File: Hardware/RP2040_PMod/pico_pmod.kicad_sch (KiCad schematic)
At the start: 39 parts, among them J1 Conn_02x06_Odd_Even, J2 Conn_02x06_Odd_Even, J3 Conn_02x06_Odd_Even, J4 USB_C_Receptacle_USB2.0, J5 Conn_01x04, SW1 SW_Push, SW2 SW_Push, U1 RP2040, U2 W25Q128JVS, U3 NCP1117-3.3_SOT223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

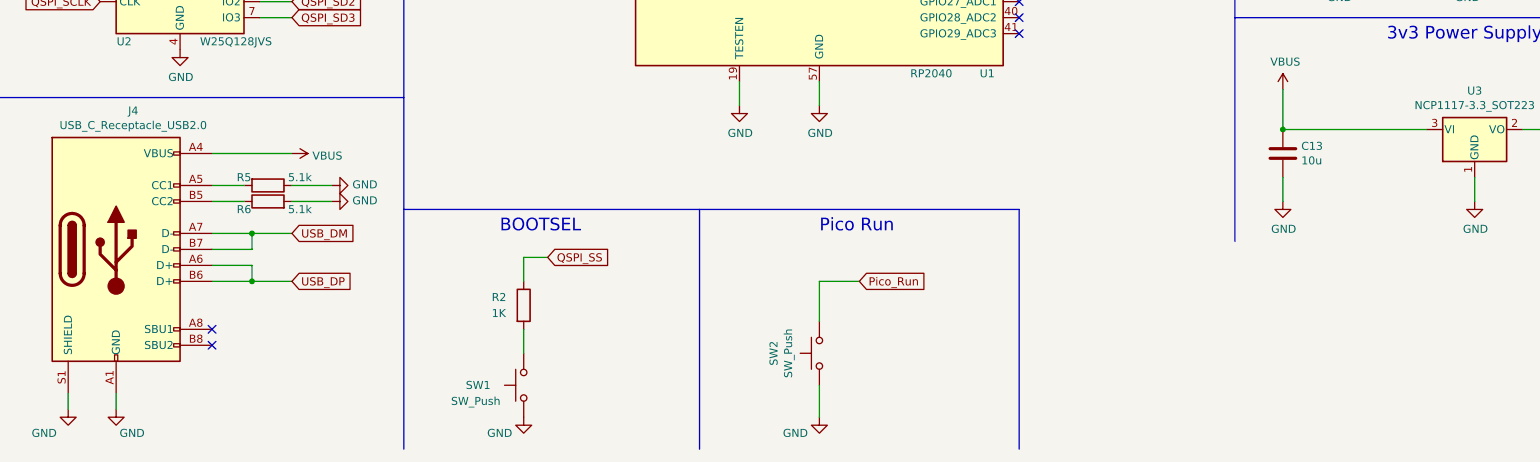
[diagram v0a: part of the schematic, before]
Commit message: add power flags to schematic for ERC
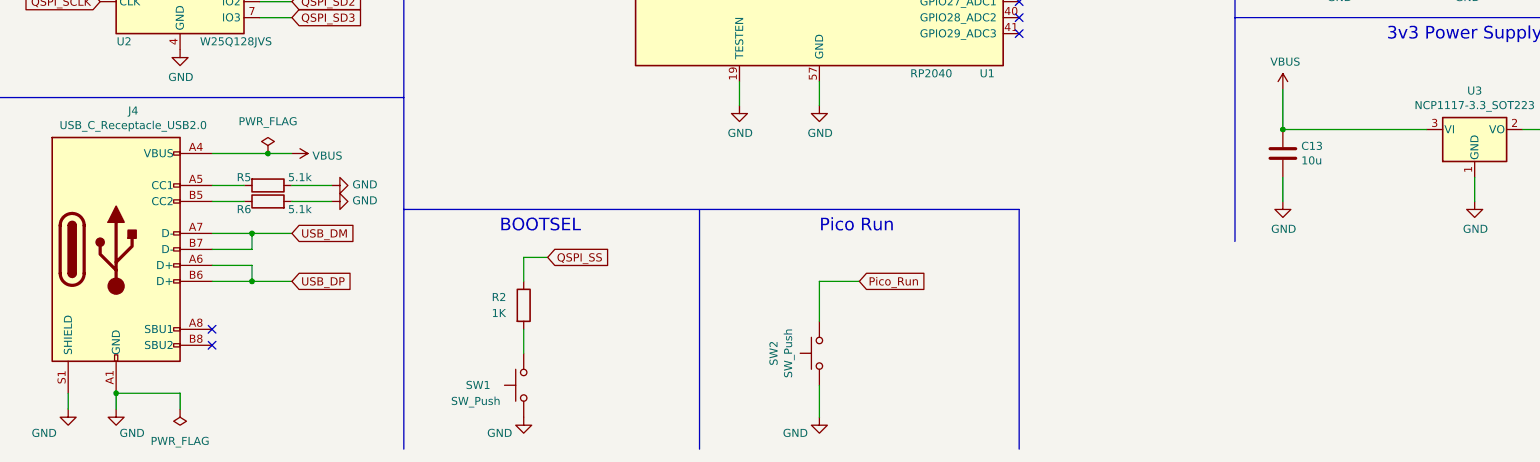
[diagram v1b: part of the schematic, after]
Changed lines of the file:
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@@
   (junction (at 33.02 78.74) (diameter 0) (color 0 0 0 0)
   )
+  (junction (at 57.15 151.13) (diameter 0) (color 0 0 0 0)
+  )
   (junction (at 26.67 102.87) (diameter 0) (color 0 0 0 0)
   )
@@
   )
   (junction (at 93.98 19.05) (diameter 0) (color 0 0 0 0)
+  )
+  (junction (at 33.02 189.23) (diameter 0) (color 0 0 0 0)
   )
   (no_connect (at 176.53 132.08))
@@
     (stroke (width 0) (type default) (color 0 0 0 0))
   )
-  (wire (pts (xy 60.96 151.13) (xy 48.26 151.13))
+  (wire (pts (xy 48.26 151.13) (xy 57.15 151.13))
     (stroke (width 0) (type default) (color 0 0 0 0))
   )
@@
     (stroke (width 0) (type default) (color 0 0 0 0))
   )
+  (wire (pts (xy 256.54 147.32) (xy 275.59 147.32))
+    (stroke (width 0) (type default) (color 0 0 0 0))
+  )
   (wire (pts (xy 255.27 22.86) (xy 264.16 22.86))
     (stroke (width 0) (type default) (color 0 0 0 0))
@@
     (stroke (width 0) (type default) (color 0 0 0 0))
   )
-  (wire (pts (xy 241.3 147.32) (xy 218.44 147.32))
-    (stroke (width 0) (type default) (color 0 0 0 0))
-  )
   (wire (pts (xy 60.96 171.45) (xy 54.61 171.45))
     (stroke (width 0) (type default) (color 0 0 0 0))
@@
     (stroke (width 0) (type default) (color 0 0 0 0))
   )
+  (wire (pts (xy 43.18 189.23) (xy 33.02 189.23))
+    (stroke (width 0) (type default) (color 0 0 0 0))
+  )
   (wire (pts (xy 124.46 38.1) (xy 124.46 21.59))
     (stroke (width 0) (type default) (color 0 0 0 0))
@@
     (stroke (width 0) (type default) (color 0 0 0 0))
   )
+  (wire (pts (xy 218.44 147.32) (xy 241.3 147.32))
+    (stroke (width 0) (type default) (color 0 0 0 0))
+  )
   (wire (pts (xy 242.57 80.01) (xy 232.41 80.01))
     (stroke (width 0) (type default) (color 0 0 0 0))
@@
     (stroke (width 0) (type default) (color 0 0 0 0))
   )
+  (wire (pts (xy 43.18 191.77) (xy 43.18 189.23))
+    (stroke (width 0) (type default) (color 0 0 0 0))
+  )
   (wire (pts (xy 127 38.1) (xy 127 20.32))
     (stroke (width 0) (type default) (color 0 0 0 0))
@@
     (stroke (width 0) (type default) (color 0 0 0 0))
   )
+  (wire (pts (xy 57.15 151.13) (xy 60.96 151.13))
+    (stroke (width 0) (type default) (color 0 0 0 0))
+  )
   (wire (pts (xy 101.6 167.64) (xy 97.79 167.64))
     (stroke (width 0) (type default) (color 0 0 0 0))
@@
   )
   (wire (pts (xy 40.64 27.94) (xy 35.56 27.94))
-    (stroke (width 0) (type default) (color 0 0 0 0))
-  )
-  (wire (pts (xy 256.54 147.32) (xy 275.59 147.32))
     (stroke (width 0) (type default) (color 0 0 0 0))
   )
@@
     (pin "1")
   )
+  (symbol (lib_id "power:PWR_FLAG") (at 57.15 151.13 0) (unit 1)
+    (in_bom yes) (on_board yes) (fields_autoplaced)
+    (property "Reference" "#FLG0102" (id 0) (at 57.15 149.225 0)
+      (effects (font (size 1.27 1.27)) hide)
+    )
+    (property "Value" "PWR_FLAG" (id 1) (at 57.15 146.05 0))
+    (property "Footprint" "" (id 2) (at 57.15 151.13 0)
+      (effects (font (size 1.27 1.27)) hide)
+    )
+    (property "Datasheet" "~" (id 3) (at 57.15 151.13 0)
+      (effects (font (size 1.27 1.27)) hide)
+    )
+    (pin "1")
+  )
+  (symbol (lib_id "power:PWR_FLAG") (at 43.18 191.77 180) (unit 1)
+    (in_bom yes) (on_board yes) (fields_autoplaced)
+    (property "Reference" "#FLG0101" (id 0) (at 43.18 193.675 0)
+      (effects (font (size 1.27 1.27)) hide)
+    )
+    (property "Value" "PWR_FLAG" (id 1) (at 43.18 196.85 0))
+    (property "Footprint" "" (id 2) (at 43.18 191.77 0)
+      (effects (font (size 1.27 1.27)) hide)
+    )
+    (property "Datasheet" "~" (id 3) (at 43.18 191.77 0)
+      (effects (font (size 1.27 1.27)) hide)
+    )
+    (pin "1")
+  )
   (sheet_instances
     (path "/" (page "1"))
   )
   (symbol_instances
+    (path "/ea875e74-ca6f-4a31-a519-44c018b1720e"
+      (reference "#FLG0101") (unit 1) (value "PWR_FLAG") (footprint "")
+    )
+    (path "/94680b10-1536-421d-a7e5-c7a3c30c89ed"
+      (reference "#FLG0102") (unit 1) (value "PWR_FLAG") (footprint "")
+    )
     (path "/00000000-0000-0000-0000-000060ea87f5"
       (reference "#PWR0101") (unit 1) (value "GND") (footprint "")

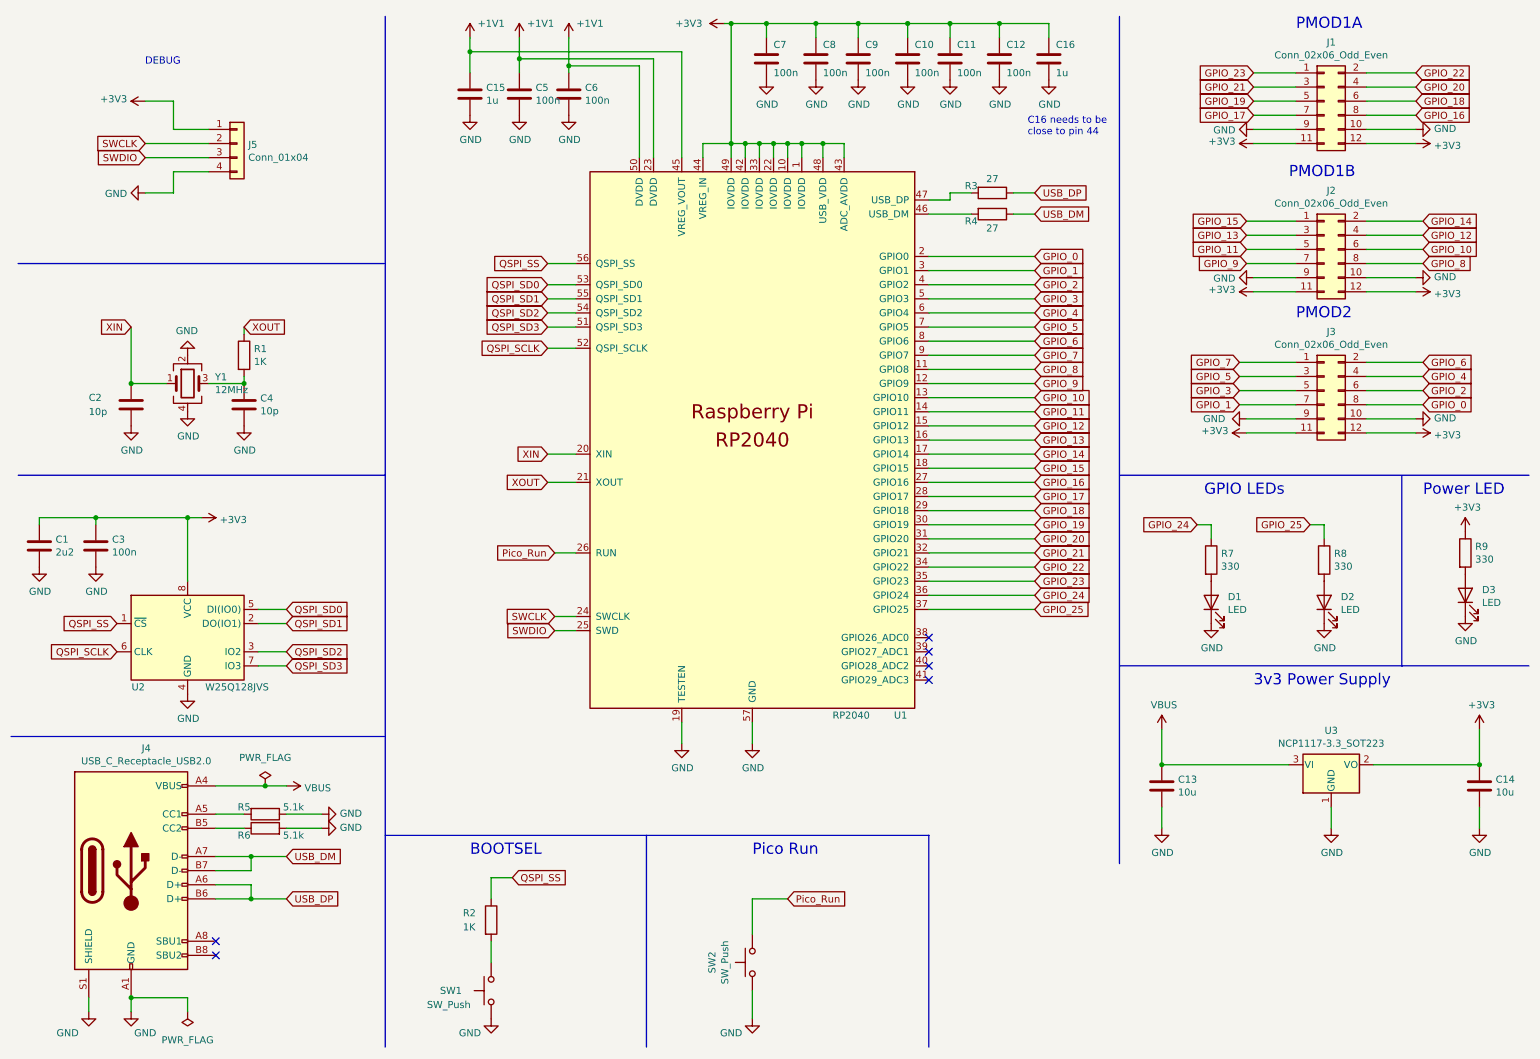
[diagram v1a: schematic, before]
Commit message: Update schematic to kicad7
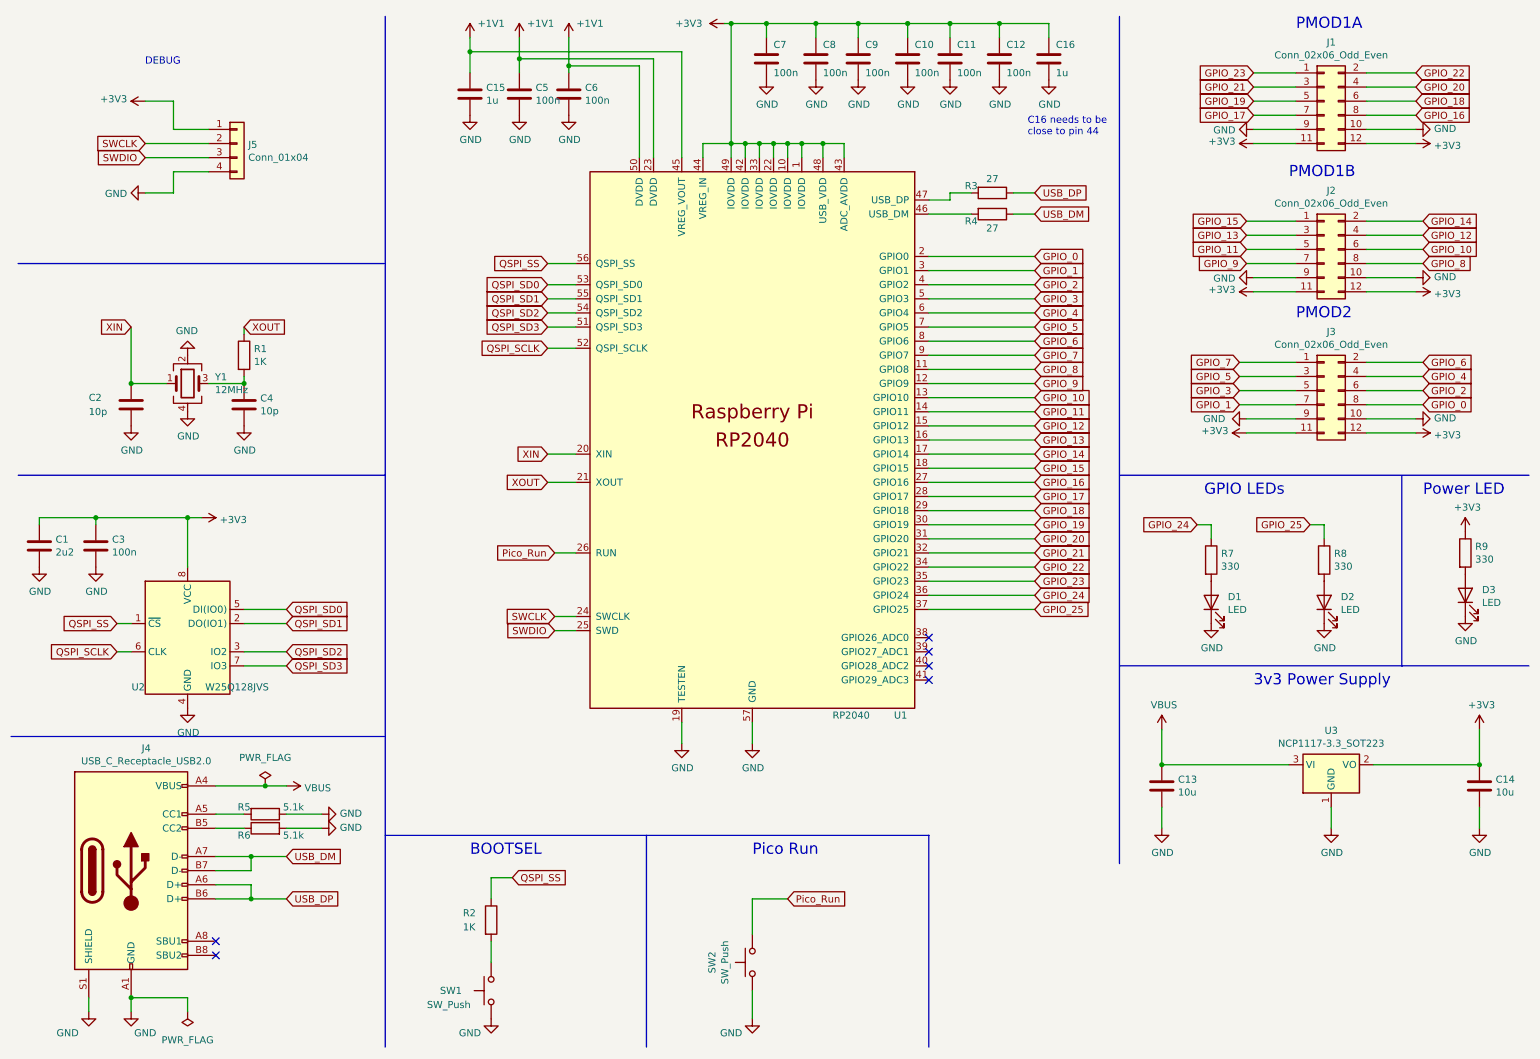
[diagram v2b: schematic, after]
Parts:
- U1: footprint RaspberryPi:RP2040-QFN-56 -> RP2040_minimal:RP2040-QFN-56

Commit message: Add JLC Part numbers
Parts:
- J1, J2, J3, J5, SW1, SW2: now left out of the parts list
- J4: JLC (none) -> C5119948
- R2: JLC (none) -> C21190
- R5, R6: JLC (none) -> C23186
- U1: JLC (none) -> C2040
- U2: JLC (none) -> C97521
- U3: JLC (none) -> C146799
- Y1: JLC (none) -> C5765982
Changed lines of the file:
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@@
+      (effects (font (size 1.27 1.27)) hide)
+    )
+    (property "JLC" "C2040" (at 144.78 88.9 0)
       (effects (font (size 1.27 1.27)) hide)
     )
@@
   )
   (symbol (lib_id "Connector_Generic:Conn_02x06_Odd_Even") (at 247.65 27.94 0) (unit 1)
-    (in_bom yes) (on_board yes) (dnp no)
+    (in_bom no) (on_board yes) (dnp no)
     (property "Reference" "J1" (at 248.92 17.3482 0)
       (effects (font (size 1.27 1.27)))
@@
   )
   (symbol (lib_id "Connector_Generic:Conn_02x06_Odd_Even") (at 247.65 54.61 0) (unit 1)
-    (in_bom yes) (on_board yes) (dnp no)
+    (in_bom no) (on_board yes) (dnp no)
     (property "Reference" "J2" (at 248.92 44.0182 0)
       (effects (font (size 1.27 1.27)))
@@
   )
   (symbol (lib_id "Connector_Generic:Conn_02x06_Odd_Even") (at 247.65 80.01 0) (unit 1)
-    (in_bom yes) (on_board yes) (dnp no)
+    (in_bom no) (on_board yes) (dnp no)
     (property "Reference" "J3" (at 248.92 69.4182 0)
       (effects (font (size 1.27 1.27)))
@@
   )
   (symbol (lib_id "Switch:SW_Push") (at 97.79 187.96 90) (unit 1)
-    (in_bom yes) (on_board yes) (dnp no)
+    (in_bom no) (on_board yes) (dnp no)
     (property "Reference" "SW1" (at 90.551 187.96 90)
       (effects (font (size 1.27 1.27)))
@@
   )
   (symbol (lib_id "Switch:SW_Push") (at 144.78 182.88 90) (unit 1)
-    (in_bom yes) (on_board yes) (dnp no)
+    (in_bom no) (on_board yes) (dnp no)
     (property "Reference" "SW2" (at 137.541 182.88 0)
       (effects (font (size 1.27 1.27)))
@@
       (effects (font (size 1.27 1.27)) hide)
     )
+    (property "JLC" "C21190" (at 97.79 175.26 0)
+      (effects (font (size 1.27 1.27)) hide)
+    )
     (pin "1")
     (pin "2")
@@
     )
     (property "Datasheet" "https://www.usb.org/sites/default/files/documents/usb_type-c.zip" (at 36.83 166.37 0)
+      (effects (font (size 1.27 1.27)) hide)
+    )
+    (property "JLC" "C5119948" (at 33.02 166.37 0)
       (effects (font (size 1.27 1.27)) hide)
     )
@@
       (effects (font (size 1.27 1.27)) hide)
     )
+    (property "JLC" "C97521" (at 43.18 124.46 0)
+      (effects (font (size 1.27 1.27)) hide)
+    )
     (pin "1")
     (pin "2")
@@
       (effects (font (size 1.27 1.27)) hide)
     )
+    (property "JLC" "C5765982" (at 43.18 78.74 0)
+      (effects (font (size 1.27 1.27)) hide)
+    )
     (pin "1")
     (pin "2")
@@
       (effects (font (size 1.27 1.27)) hide)
     )
+    (property "JLC" "C146799" (at 248.92 147.32 0)
+      (effects (font (size 1.27 1.27)) hide)
+    )
     (pin "1")
     (pin "2")
@@
       (effects (font (size 1.27 1.27)) hide)
     )
+    (property "JLC" "C23186" (at 57.15 156.21 90)
+      (effects (font (size 1.27 1.27)) hide)
+    )
     (pin "1")
     (pin "2")
@@
     )
     (property "Datasheet" "~" (at 57.15 158.75 0)
+      (effects (font (size 1.27 1.27)) hide)
+    )
+    (property "JLC" "C23186" (at 57.15 158.75 90)
       (effects (font (size 1.27 1.27)) hide)
     )
@@
   )
   (symbol (lib_id "Connector_Generic:Conn_01x04") (at 52.07 35.56 0) (unit 1)
-    (in_bom yes) (on_board yes) (dnp no)
+    (in_bom no) (on_board yes) (dnp no)
     (property "Reference" "J5" (at 54.102 35.7632 0)
       (effects (font (size 1.27 1.27)) (justify left))

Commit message: Add JLC Part numbers
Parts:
- C1: JLC (none) -> C23630
- C10, C11, C12, C3, C5, C6, C7, C8, C9: JLC (none) -> C14663
- C13, C14: JLC (none) -> C19702
- C15, C16: JLC (none) -> C15849
- C2, C4: JLC (none) -> C1634
- D1, D2, D3: JLC (none) -> C2286
- R7, R8, R9: JLC (none) -> C23138
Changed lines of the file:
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@@
+      (effects (font (size 1.27 1.27)) hide)
+    )
+    (property "JLC" "C14663" (at 26.67 107.95 0)
       (effects (font (size 1.27 1.27)) hide)
     )
@@
       (effects (font (size 1.27 1.27)) hide)
     )
+    (property "JLC" "C23630" (at 16.51 107.95 0)
+      (effects (font (size 1.27 1.27)) hide)
+    )
     (pin "1")
     (pin "2")
@@
       (effects (font (size 1.27 1.27)) hide)
     )
+    (property "JLC" "C19702" (at 275.59 151.13 0)
+      (effects (font (size 1.27 1.27)) hide)
+    )
     (pin "1")
     (pin "2")
@@
       (effects (font (size 1.27 1.27)) hide)
     )
+    (property "JLC" "C19702" (at 218.44 151.13 0)
+      (effects (font (size 1.27 1.27)) hide)
+    )
     (pin "1")
     (pin "2")
@@
       (effects (font (size 1.27 1.27)) hide)
     )
+    (property "JLC" "C15849" (at 93.98 26.67 0)
+      (effects (font (size 1.27 1.27)) hide)
+    )
     (pin "1")
     (pin "2")
@@
     )
     (property "Datasheet" "~" (at 198.12 20.32 0)
+      (effects (font (size 1.27 1.27)) hide)
+    )
+    (property "JLC" "C15849" (at 198.12 20.32 0)
       (effects (font (size 1.27 1.27)) hide)
     )
@@
       (effects (font (size 1.27 1.27)) hide)
     )
+    (property "JLC" "C1634" (at 33.02 82.55 0)
+      (effects (font (size 1.27 1.27)) hide)
+    )
     (pin "1")
     (pin "2")
@@
       (effects (font (size 1.27 1.27)) hide)
     )
+    (property "JLC" "C1634" (at 53.34 82.55 0)
+      (effects (font (size 1.27 1.27)) hide)
+    )
     (pin "1")
     (pin "2")
@@
     )
     (property "Datasheet" "~" (at 227.33 110.49 0)
+      (effects (font (size 1.27 1.27)) hide)
+    )
+    (property "JLC" "C23138" (at 227.33 110.49 0)
       (effects (font (size 1.27 1.27)) hide)
     )
@@
       (effects (font (size 1.27 1.27)) hide)
     )
+    (property "JLC" "C2286" (at 227.33 118.11 90)
+      (effects (font (size 1.27 1.27)) hide)
+    )
     (pin "1")
     (pin "2")
@@
     )
     (property "Datasheet" "~" (at 247.65 110.49 0)
+      (effects (font (size 1.27 1.27)) hide)
+    )
+    (property "JLC" "C23138" (at 247.65 110.49 0)
       (effects (font (size 1.27 1.27)) hide)
     )
@@
       (effects (font (size 1.27 1.27)) hide)
     )
+    (property "JLC" "C2286" (at 247.65 118.11 90)
+      (effects (font (size 1.27 1.27)) hide)
+    )
     (pin "1")
     (pin "2")
@@
     )
     (property "Datasheet" "~" (at 273.05 109.22 0)
+      (effects (font (size 1.27 1.27)) hide)
+    )
+    (property "JLC" "C23138" (at 273.05 109.22 0)
       (effects (font (size 1.27 1.27)) hide)
     )
@@
       (effects (font (size 1.27 1.27)) hide)
     )
+    (property "JLC" "C2286" (at 273.05 116.84 90)
+      (effects (font (size 1.27 1.27)) hide)
+    )
     (pin "1")
     (pin "2")
@@
       (effects (font (size 1.27 1.27)) hide)
     )
+    (property "JLC" "C14663" (at 102.87 26.67 0)
+      (effects (font (size 1.27 1.27)) hide)
+    )
     (pin "1")
     (pin "2")
@@
       (effects (font (size 1.27 1.27)) hide)
     )
+    (property "JLC" "C14663" (at 111.76 26.67 0)
+      (effects (font (size 1.27 1.27)) hide)
+    )
     (pin "1")
     (pin "2")
@@
       (effects (font (size 1.27 1.27)) hide)
     )
+    (property "JLC" "C14663" (at 147.32 20.32 0)
+      (effects (font (size 1.27 1.27)) hide)
+    )
     (pin "1")
     (pin "2")
@@
       (effects (font (size 1.27 1.27)) hide)
     )
+    (property "JLC" "C14663" (at 156.21 20.32 0)
+      (effects (font (size 1.27 1.27)) hide)
+    )
     (pin "1")
     (pin "2")
@@
       (effects (font (size 1.27 1.27)) hide)
     )
+    (property "JLC" "C14663" (at 163.83 20.32 0)
+      (effects (font (size 1.27 1.27)) hide)
+    )
     (pin "1")
     (pin "2")
@@
       (effects (font (size 1.27 1.27)) hide)
     )
+    (property "JLC" "C14663" (at 172.72 20.32 0)
+      (effects (font (size 1.27 1.27)) hide)
+    )
     (pin "1")
     (pin "2")
@@
       (effects (font (size 1.27 1.27)) hide)
     )
+    (property "JLC" "C14663" (at 180.34 20.32 0)
+      (effects (font (size 1.27 1.27)) hide)
+    )
     (pin "1")
     (pin "2")
@@
       (effects (font (size 1.27 1.27)) hide)
     )
+    (property "JLC" "C14663" (at 189.23 20.32 0)
+      (effects (font (size 1.27 1.27)) hide)
+    )

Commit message: change to use LCSC part number
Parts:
- U1: JLC C2040 -> (none); LCSC# (none) -> C2040
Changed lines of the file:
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@@
       (effects (font (size 1.27 1.27)) hide)
     )
-    (property "JLC" "C2040" (at 144.78 88.9 0)
+    (property "LCSC#" "C2040" (at 144.78 88.9 0)
       (effects (font (size 1.27 1.27)) hide)
     )
